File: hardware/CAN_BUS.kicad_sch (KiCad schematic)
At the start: 15 parts, among them U7 ADM3057ExRW

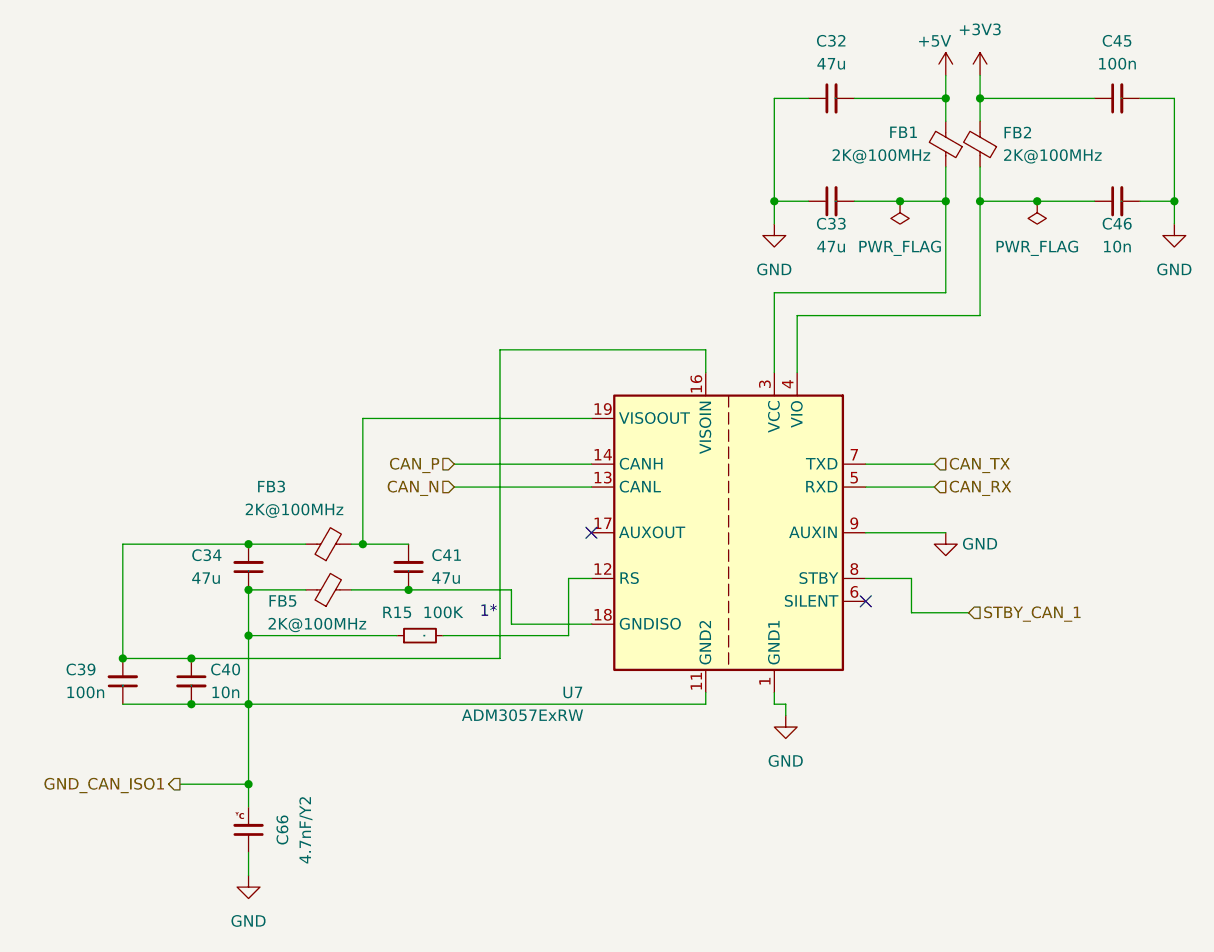
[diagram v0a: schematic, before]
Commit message: changed out of stock parts
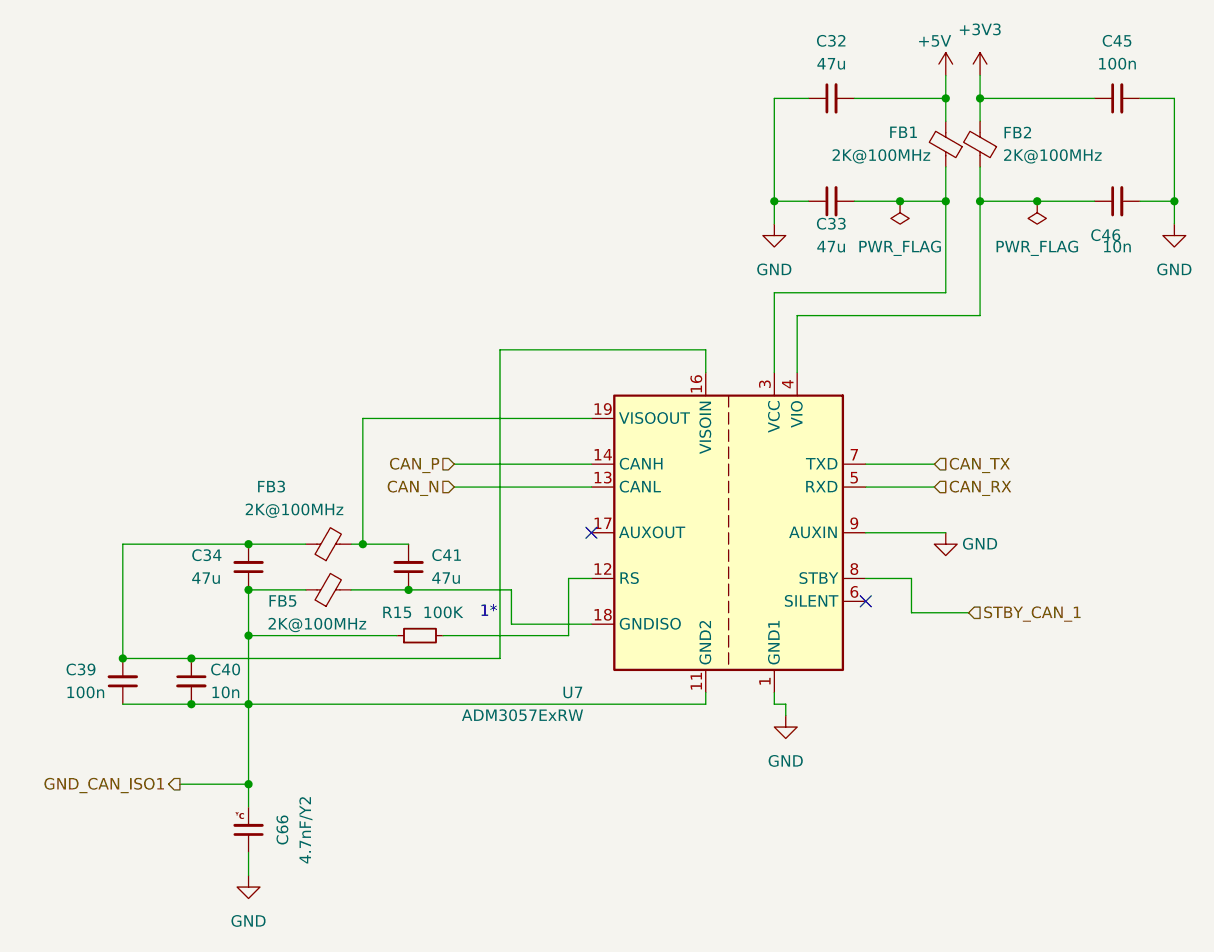
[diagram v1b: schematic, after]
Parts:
- C32, C33, C34, C41: Mouser Part Number . -> 81-GRM21BR60J476M01L; Mouser price/stock (none) -> https://www.mouser.pl/pl/ProductDetail/Murata-Electronics/G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
- C39, C45: Mouser Part Number . -> 963-MAJCU168BB7104KT; Mouser price/stock (none) -> https://www.mouser.pl/pl/ProductDetail/TAIYO-YUDEN/MAJCU168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
- C40, C46: Mouser Part Number . -> 81-GCJ188R71E103KA1D; Mouser price/stock (none) -> https://www.mouser.pl/pl/ProductDetail/Murata-Electronics/G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
- FB1, FB2, FB3, FB5: Mouser price / stock (none) -> https://www.mouser.pl/pl/ProductDetail/Fair-Rite/2508052027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
- R15: Mouser Part Number . -> 279-1-72225-5; Mouser price / stock (none) -> https://www.mouser.pl/pl/ProductDetail/TE-Connectivity-Hols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
- U7: Mouser priice/stock (none) -> https://www.mouser.pl/pl/ProductDetail/Analog-Devices/ADM30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
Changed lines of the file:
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@@
+			)
+		)
+		(property "Mouser price / stock" "https://www.mouser.pl/pl/ProductDetail/Fair-Rite/2508052027Y1?qs=paL1wOLBYNcCgyNDp2sTMQ%3D%3D"
+			(at 99.06 102.87 90)
+			(hide yes)
+			(show_name no)
+			(do_not_autoplace no)
+			(effects
+				(font
+					(size 1.27 1.27)
+				)
 			)
 		)
@@
 			)
 		)
+		(property "Mouser price / stock" "https://www.mouser.pl/pl/ProductDetail/Fair-Rite/2508052027Y1?qs=paL1wOLBYNcCgyNDp2sTMQ%3D%3D"
+			(at 167.64 53.34 0)
+			(hide yes)
+			(show_name no)
+			(do_not_autoplace no)
+			(effects
+				(font
+					(size 1.27 1.27)
+				)
+			)
+		)
 		(pin "2"
 		)
@@
 			)
 		)
-		(property "Datasheet" ""
+		(property "Datasheet" "https://www.mouser.pl/datasheet/3/76/4/GRM21BR60J476ME01_01A.pdf"
 			(at 154.94 59.69 0)
 			(hide yes)
@@
 			)
 		)
-		(property "Mouser Part Number" "."
+		(property "Mouser Part Number" "81-GRM21BR60J476M01L"
 			(at 154.94 59.69 0)
+			(hide yes)
+			(show_name no)
+			(do_not_autoplace no)
+			(effects
+				(font
+					(size 1.27 1.27)
+				)
+			)
+		)
+		(property "Mouser price/stock" "https://www.mouser.pl/pl/ProductDetail/Murata-Electronics/GRM21BR60J476ME01L?qs=u16ybLDytRYYQtTToF3RWA%3D%3D"
+			(at 154.94 59.69 90)
+			(hide yes)
 			(show_name no)
 			(do_not_autoplace no)
@@
 			)
 		)
-		(property "Datasheet" ""
+		(property "Datasheet" "https://www.mouser.pl/datasheet/3/76/4/GRM21BR60J476ME01_01A.pdf"
 			(at 90.17 100.33 0)
 			(hide yes)
@@
 			)
 		)
-		(property "Mouser Part Number" "."
+		(property "Mouser Part Number" "81-GRM21BR60J476M01L"
 			(at 90.17 100.33 0)
+			(hide yes)
+			(show_name no)
+			(do_not_autoplace no)
+			(effects
+				(font
+					(size 1.27 1.27)
+				)
+			)
+		)
+		(property "Mouser price/stock" "https://www.mouser.pl/pl/ProductDetail/Murata-Electronics/GRM21BR60J476ME01L?qs=u16ybLDytRYYQtTToF3RWA%3D%3D"
+			(at 90.17 100.33 0)
+			(hide yes)
 			(show_name no)
 			(do_not_autoplace no)
@@
 			)
 		)
-		(property "Datasheet" ""
+		(property "Datasheet" "https://www.mouser.pl/datasheet/3/76/4/GRM21BR60J476ME01_01A.pdf"
 			(at 154.94 48.26 0)
 			(hide yes)
@@
 			)
 		)
-		(property "Mouser Part Number" "."
+		(property "Mouser Part Number" "81-GRM21BR60J476M01L"
 			(at 154.94 48.26 0)
+			(hide yes)
+			(show_name no)
+			(do_not_autoplace no)
+			(effects
+				(font
+					(size 1.27 1.27)
+				)
+			)
+		)
+		(property "Mouser price/stock" "https://www.mouser.pl/pl/ProductDetail/Murata-Electronics/GRM21BR60J476ME01L?qs=u16ybLDytRYYQtTToF3RWA%3D%3D"
+			(at 154.94 48.26 90)
+			(hide yes)
 			(show_name no)
 			(do_not_autoplace no)
@@
 			)
 		)
-		(property "Datasheet" ""
+		(property "Datasheet" "https://www.mouser.pl/datasheet/3/76/4/GRM21BR60J476ME01_01A.pdf"
 			(at 107.95 100.33 0)
 			(hide yes)
@@
 			)
 		)
-		(property "Mouser Part Number" "."
+		(property "Mouser Part Number" "81-GRM21BR60J476M01L"
 			(at 107.95 100.33 0)
+			(hide yes)
+			(show_name no)
+			(do_not_autoplace no)
+			(effects
+				(font
+					(size 1.27 1.27)
+				)
+			)
+		)
+		(property "Mouser price/stock" "https://www.mouser.pl/pl/ProductDetail/Murata-Electronics/GRM21BR60J476ME01L?qs=u16ybLDytRYYQtTToF3RWA%3D%3D"
+			(at 107.95 100.33 0)
+			(hide yes)
 			(show_name no)
 			(do_not_autoplace no)
@@
 		(dnp no)
 		(property "Reference" "C46"
-			(at 186.69 62.23 90)
+			(at 185.42 63.5 90)
 			(show_name no)
 			(do_not_autoplace no)
@@
 			)
 		)
-		(property "Datasheet" ""
+		(property "Datasheet" "https://www.mouser.pl/datasheet/3/76/2/GCJ188R71E103KA01_02D.pdf"
 			(at 186.69 59.69 0)
 			(hide yes)
@@
 			)
 		)
-		(property "Mouser Part Number" "."
-			(at 186.69 59.69 0)
+		(property "Mouser Part Number" "81-GCJ188R71E103KA1D"
+			(at 184.15 60.96 0)
+			(hide yes)
+			(show_name no)
+			(do_not_autoplace no)
+			(effects
+				(font
+					(size 1.27 1.27)
+				)
+			)
+		)
+		(property "Mouser price/stock" "https://www.mouser.pl/pl/ProductDetail/Murata-Electronics/GCJ188R71E103KA01D?qs=VNXXsjD6WfWpkebh3gRilw%3D%3D"
+			(at 186.69 59.69 90)
+			(hide yes)
 			(show_name no)
 			(do_not_autoplace no)
@@
 			)
 		)
+		(property "Mouser priice/stock" "https://www.mouser.pl/pl/ProductDetail/Analog-Devices/ADM3057EBRWZ?qs=PqoDHHvF649%2FWAcdgp0Vvw%3D%3D"
+			(at 143.51 96.52 0)
+			(hide yes)
+			(show_name no)
+			(do_not_autoplace no)
+			(effects
+				(font
+					(size 1.27 1.27)
+				)
+			)
+		)
 		(pin "5"
 		)
@@
 		)
 		(property "Mouser Part Number" "623-2508052027Y1"
+			(at 171.45 53.34 0)
+			(hide yes)
+			(show_name no)
+			(do_not_autoplace no)
+			(effects
+				(font
+					(size 1.27 1.27)
+				)
+			)
+		)
+		(property "Mouser price / stock" "https://www.mouser.pl/pl/ProductDetail/Fair-Rite/2508052027Y1?qs=paL1wOLBYNcCgyNDp2sTMQ%3D%3D"
 			(at 171.45 53.34 0)
 			(hide yes)
@@
 			)
 		)
-		(property "Mouser Part Number" "."
-			(at 109.22 107.95 0)
+		(property "Mouser Part Number" "279-1-72225-5"
+			(at 111.76 107.95 0)
+			(hide yes)
+			(show_name no)
+			(do_not_autoplace no)
+			(effects
+				(font
+					(size 1.27 1.27)
+				)
+			)
+		)
+		(property "Mouser price / stock" "https://www.mouser.pl/pl/ProductDetail/TE-Connectivity-Holsworthy/CRGSP0603F100K?qs=Naspt24KZtlrfquNf0AL%252BQ%3D%3D"
+			(at 109.22 107.95 90)
+			(hide yes)
 			(show_name no)
 			(do_not_autoplace no)
@@
 			)
 		)
-		(property "Datasheet" ""
+		(property "Datasheet" "https://www.mouser.com/catalog/specsheets/TAIYO_YUDEN_03-08-2024_MAJCU168BB7104KTEA01_SS.pdf"
 			(at 76.2 113.03 0)
 			(hide yes)
@@
 			)
 		)
-		(property "Mouser Part Number" "."
+		(property "Mouser Part Number" "963-MAJCU168BB7104KT"
 			(at 76.2 113.03 0)
+			(hide yes)
+			(show_name no)
+			(do_not_autoplace no)
+			(effects
+				(font
+					(size 1.27 1.27)
+				)
+			)
+		)
+		(property "Mouser price/stock" "https://www.mouser.pl/pl/ProductDetail/TAIYO-YUDEN/MAJCU168BB7104KTEA01?qs=ZcfC38r4PovJ4zMRJqa98Q%3D%3D"
+			(at 76.2 113.03 0)
+			(hide yes)
 			(show_name no)
 			(do_not_autoplace no)
@@
 			)
 		)
-		(property "Mouser Part Number" "."
+		(property "Mouser Part Number" "81-GCJ188R71E103KA1D"
+			(at 82.55 110.49 0)
+			(hide yes)
+			(show_name no)
+			(do_not_autoplace no)
+			(effects
+				(font
+					(size 1.27 1.27)
+				)
+			)
+		)
+		(property "Mouser price/stock" "https://www.mouser.pl/pl/ProductDetail/Murata-Electronics/GCJ188R71E103KA01D?qs=VNXXsjD6WfWpkebh3gRilw%3D%3D"
 			(at 83.82 113.03 0)
+			(hide yes)
 			(show_name no)
 			(do_not_autoplace no)
@@
 		(property "Mouser Part Number" "623-2508052027Y1"
 			(at 99.06 97.79 0)
+			(hide yes)
+			(show_name no)
+			(do_not_autoplace no)
+			(effects
+				(font
+					(size 1.27 1.27)
+				)
+			)
+		)
+		(property "Mouser price / stock" "https://www.mouser.pl/pl/ProductDetail/Fair-Rite/2508052027Y1?qs=paL1wOLBYNcCgyNDp2sTMQ%3D%3D"
+			(at 99.06 97.79 90)
 			(hide yes)
 			(show_name no)
@@
 			)
 		)
-		(property "Datasheet" ""
+		(property "Datasheet" "https://www.mouser.com/catalog/specsheets/TAIYO_YUDEN_03-08-2024_MAJCU168BB7104KTEA01_SS.pdf"
 			(at 186.69 48.26 0)
 			(hide yes)
@@
 			)
 		)
-		(property "Mouser Part Number" "."
+		(property "Mouser Part Number" "963-MAJCU168BB7104KT"
 			(at 186.69 48.26 0)
-			(show_name no)
-			(do_not_autoplace no)
+			(hide yes)
+			(show_name no)
+			(do_not_autoplace no)
+			(effects
+				(font
+					(size 1.27 1.27)
+				)
+			)
+		)
+		(property "Mouser price/stock" "https://www.mouser.pl/pl/ProductDetail/TAIYO-YUDEN/MAJCU168BB7104KTEA01?qs=ZcfC38r4PovJ4zMRJqa98Q%3D%3D"
+			(at 186.69 48.26 90)
+			(hide yes)
+			(show_name no)
+			(do_not_autoplace no)

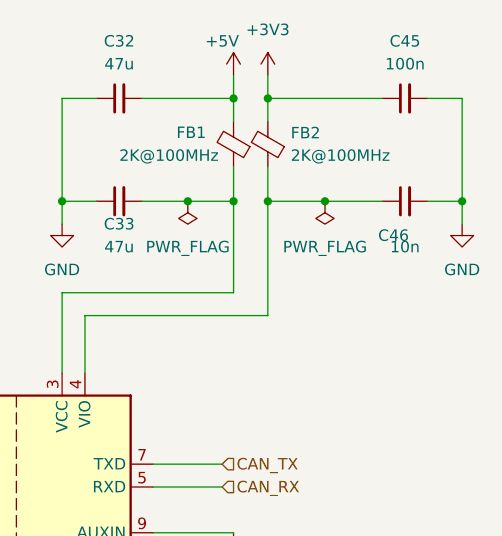
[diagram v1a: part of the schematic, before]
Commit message: fixed mouser links
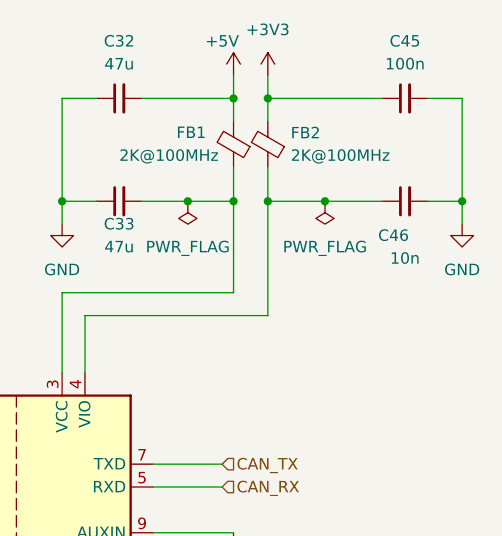
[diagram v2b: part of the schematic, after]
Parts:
- R15: Mouser Part Number 279-1-72225-5 -> 660-RK73B1JTTD104J; Mouser price / stock https://www.mouser.pl/pl/ProductDetail/TE-Connectivity-Hols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 -> https://www.mouser.pl/en/ProductDetail/KOA-Speer/RK73B1JTTD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
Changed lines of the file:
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@@
 		)
 		(property "Value" "10n"
-			(at 186.69 64.77 90)
+			(at 186.69 66.04 90)
 			(show_name no)
 			(do_not_autoplace no)
@@
 			)
 		)
-		(property "Datasheet" ""
+		(property "Datasheet" "https://www.koaspeer.com/pdfs/RK73B.pdf"
 			(at 109.22 107.95 0)
 			(hide yes)
@@
 			)
 		)
-		(property "Mouser Part Number" "279-1-72225-5"
+		(property "Mouser Part Number" "660-RK73B1JTTD104J"
 			(at 111.76 107.95 0)
 			(hide yes)
@@
 			)
 		)
-		(property "Mouser price / stock" "https://www.mouser.pl/pl/ProductDetail/TE-Connectivity-Holsworthy/CRGSP0603F100K?qs=Naspt24KZtlrfquNf0AL%252BQ%3D%3D"
+		(property "Mouser price / stock" "https://www.mouser.pl/en/ProductDetail/KOA-Speer/RK73B1JTTD104J?qs=sGAEpiMZZMvdGkrng054t2HaaJFon%252B0pQ1vDU7rpyKc%3D"
 			(at 109.22 107.95 90)
 			(hide yes)
